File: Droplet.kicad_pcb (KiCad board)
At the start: 2 copper layers, 32.8 x 16.2 mm, 31 parts, among them Q1 BSS138W_C28646265, Q2 BSS138W_C28646265, Q3 BSS138W_C28646265, Q4 BSS138W_C28646265, U1 ATtiny202-SSNR, U2 IRM-H638T/TR2, U3 PAM2803AAF095, U4 MBKK1608T1R5M

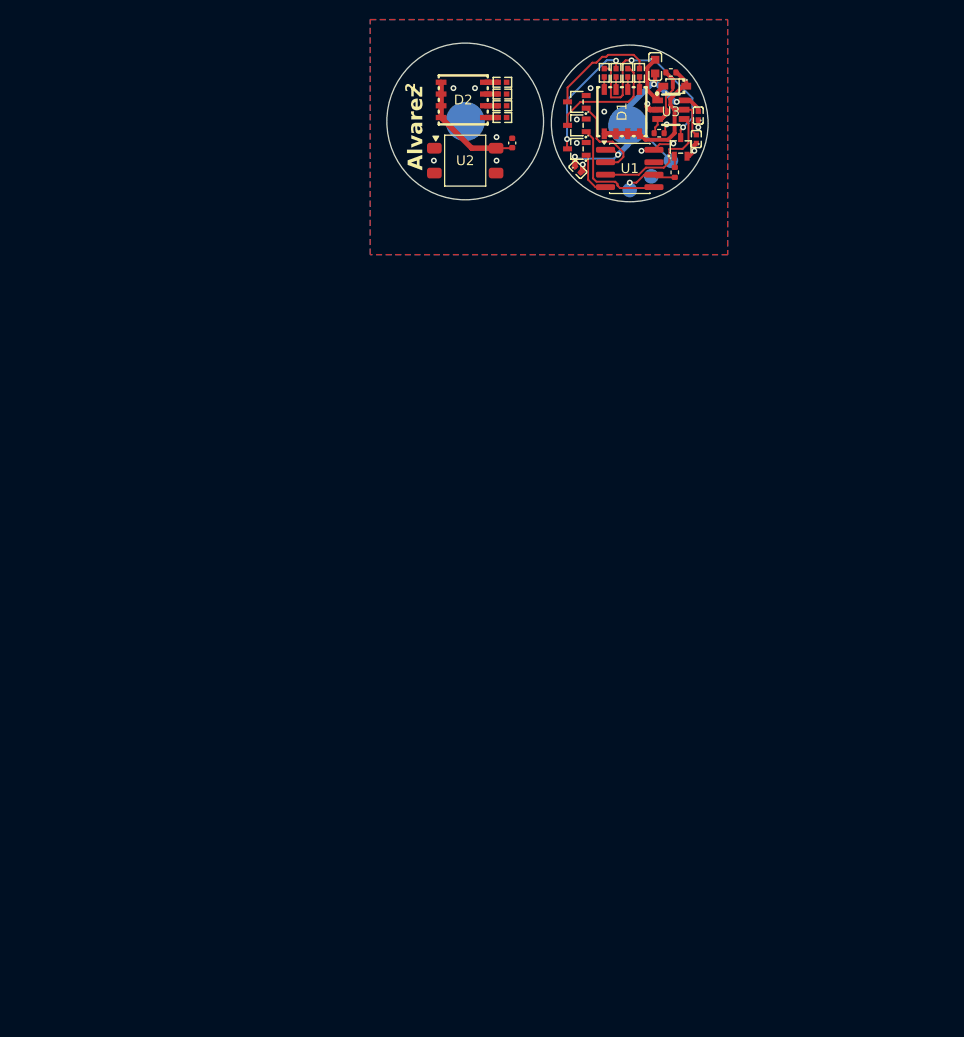
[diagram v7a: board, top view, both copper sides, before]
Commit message: add boost, rework for flex pcb, order
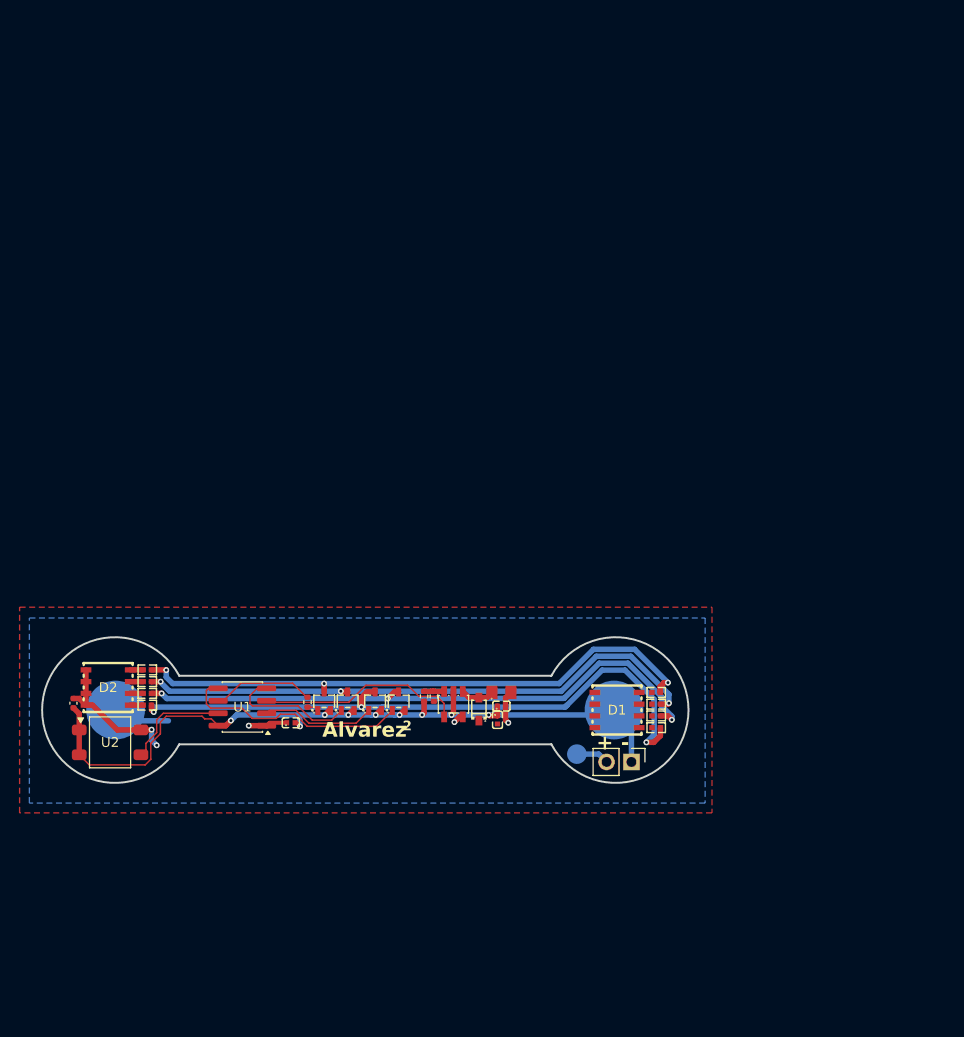
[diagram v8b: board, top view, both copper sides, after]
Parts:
- removed TP4: GND, TestPoint:TestPoint_Pad_D1.5mm
- removed TP5: V+, TestPoint:TestPoint_Pad_D1.5mm
- removed U4: MBKK1608T1R5M, easyeda2kicad:L0603
- added J1: Conn_01x02_Pin, Connector_PinHeader_2.54mm:PinHeader_1x02_P2.54mm_Vertical, F.Cu at (131.2, 94.8)
- added L1: MPL2012S4R7MHT, easyeda2kicad:L0805, F.Cu at (117.9, 87.7)
- R10: value 4.7k -> 100k
- R9: value 51k -> 200k
- TP1, TP2: footprint TestPoint:TestPoint_Pad_D4.0mm -> TestPoint:TestPoint_Pad_D6.0mm
- TP3: value PA0 -> +; footprint TestPoint:TestPoint_Pad_D1.5mm -> TestPoint:TestPoint_Pad_D2.0mm
- U3: value PAM2803AAF095 -> MT3540-F23; footprint easyeda2kicad:SOT-23-6_L2.9-W1.6-P0.95-LS2.8-BR -> easyeda2kicad:SOT-23-5_L3.0-W1.7-P0.95-LS2.8-BR
- moved TP1 79.4 mm to (78.5, 89.5)
- moved C2 72.7 mm to (74.2, 88.8), turned to -90 degrees
- moved D2 70.1 mm to (77.7, 87.2)
- moved R3 70.1 mm to (81.7, 89.0)
- moved R1 70.1 mm to (81.7, 86.6)
- moved R2 70.1 mm to (81.7, 87.8)
- moved R7 70.1 mm to (81.7, 85.4)
- moved U2 69.6 mm to (77.9, 92.8)
- moved R9 68.1 mm to (111.0, 88.1), turned to 90 degrees
- moved U1 67.7 mm to (91.5, 89.2), turned to 180 degrees
- moved Q1 67.3 mm to (99.8, 88.6)
- moved R6 66.9 mm to (133.7, 91.3), turned to 180 degrees
- moved D3 66.7 mm to (115.6, 89.4), turned to 90 degrees
- moved R11 65.8 mm to (98.1, 88.7), turned to 90 degrees
- moved R5 65.7 mm to (133.7, 90.1), turned to 180 degrees
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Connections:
- TP3 pad 1: /PA0 -> VBATT
- U3 pad 5: /VREG -> VBATT
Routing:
- net GND: track 8.97 -> 82.5 mm, vias 16 -> 9
- net /white: track 11.2 -> 64.7 mm, vias 0 -> 3
- net /blue: track 11.8 -> 60.7 mm, vias 0 -> 3
- net /green: track 12.6 -> 58.9 mm, vias 2 -> 3
- net /red: track 21.4 -> 59.0 mm, vias 2 -> 3
- net /VREG: track 33.1 -> 14.7 mm, vias 0 -> 2
- net VBATT: track 30.0 -> 18.0 mm, vias 4 -> 3
- net /PA2: track 11.8 -> 23.6 mm
- net /PA3: track 0.00 -> 11.6 mm
- net /PA1: track 4.67 -> 13.2 mm
- net /PA7: track 13.2 -> 21.1 mm
- net Net-(U3-FB): track 7.61 -> 2.25 mm
- net /PA0: track 5.80 -> 10.4 mm, vias 1 -> 0
- net Net-(D3-A): track 6.61 -> 3.46 mm
- net /PA6: track 9.37 -> 11.6 mm
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- added copper zone on F.Cu, net /VREG
- added copper zone on B.Cu, net VBATT
- removed copper zone on B.Cu, net GND
- removed copper zone on F.Cu, net GND
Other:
- board size 32.8 x 16.2 mm -> 66 x 14.9 mm
- board text added: "+"
- board text added: "-"
- board text added: "Bat -"
- board text added: "Bat+"
- board text removed: "BAT+"
- board text removed: "BAT-"
